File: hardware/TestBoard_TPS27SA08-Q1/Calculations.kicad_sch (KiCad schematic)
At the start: 0 parts

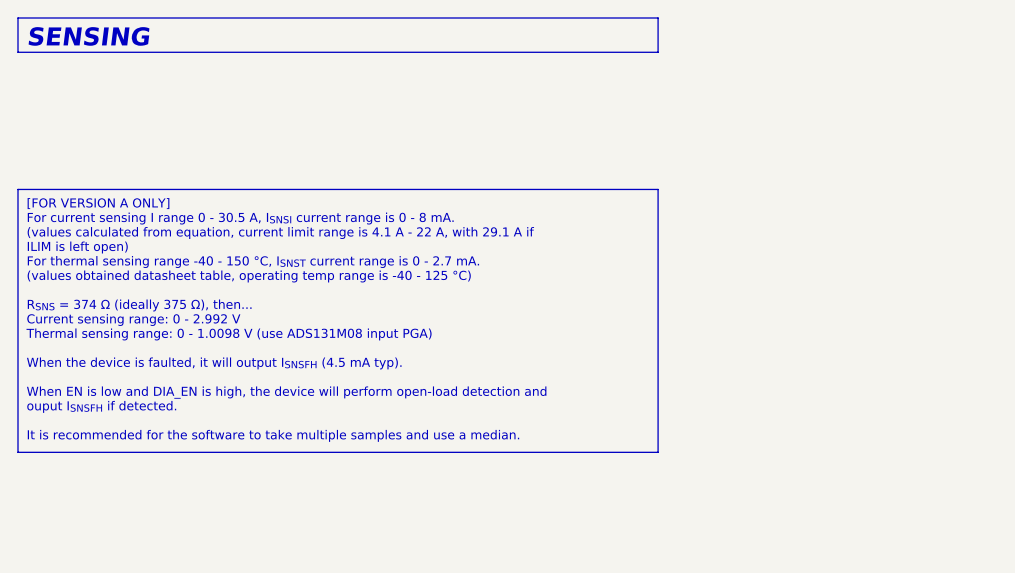
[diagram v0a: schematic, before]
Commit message: revisions (dip switch for address, leds on gpio outputs, logic analyzer pinout?, ...)
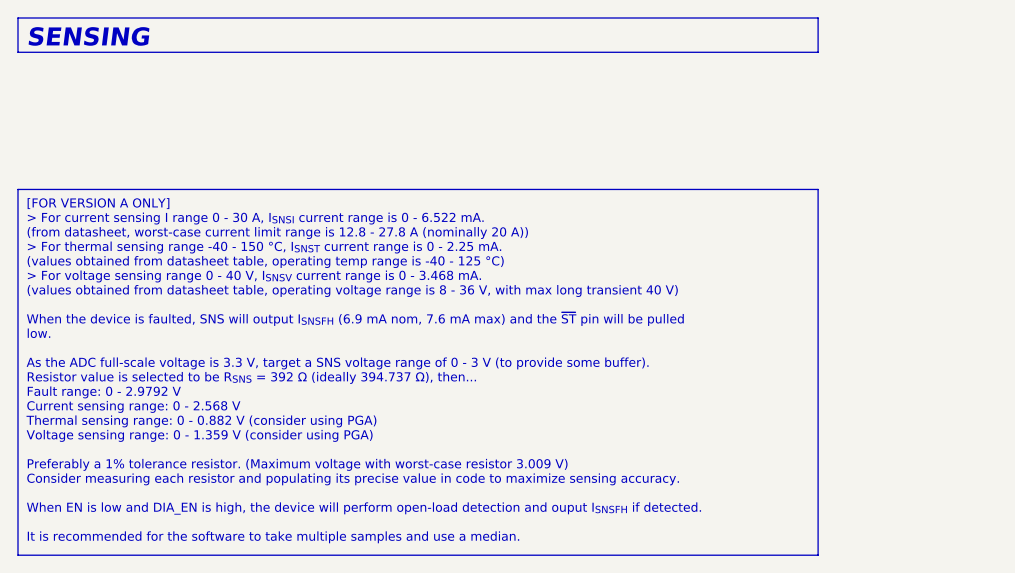
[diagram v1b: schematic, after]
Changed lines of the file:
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@@
 		(exclude_from_sim no)
 		(at 16.51 15.24 0)
-		(size 71.12 3.81)
+		(size 88.9 3.81)
 		(margins 0.9525 0.9525 0.9525 0.9525)
 		(stroke
@@
 		)
 	)
-	(text_box "[FOR VERSION A ONLY]\nFor current sensing I range 0 - 30.5 A, I_{SNSI} current range is 0 - 8 mA. \n(values calculated from equation, current limit range is 4.1 A - 22 A, with 29.1 A if ILIM is left open)\nFor thermal sensing range -40 - 150 °C, I_{SNST} current range is 0 - 2.7 mA. \n(values obtained datasheet table, operating temp range is -40 - 125 °C)\n\nR_{SNS} = 374 Ω (ideally 375 Ω), then...\nCurrent sensing range: 0 - 2.992 V\nThermal sensing range: 0 - 1.0098 V (use ADS131M08 input PGA)\n\nWhen the device is faulted, it will output I_{SNSFH} (4.5 mA typ). \n\nWhen EN is low and DIA_EN is high, the device will perform open-load detection and ouput I_{SNSFH} if detected.\n\nIt is recommended for the software to take multiple samples and use a median."
+	(text_box "[FOR VERSION A ONLY]\n> For current sensing I range 0 - 30 A, I_{SNSI} current range is 0 - 6.522 mA. \n  (from datasheet, worst-case current limit range is 12.8 - 27.8 A (nominally 20 A))\n> For thermal sensing range -40 - 150 °C, I_{SNST} current range is 0 - 2.25 mA. \n  (values obtained from datasheet table, operating temp range is -40 - 125 °C)\n> For voltage sensing range 0 - 40 V, I_{SNSV} current range is 0 - 3.468 mA. \n  (values obtained from datasheet table, operating voltage range is 8 - 36 V, with max long transient 40 V)\n\nWhen the device is faulted, SNS will output I_{SNSFH} (6.9 mA nom, 7.6 mA max) and the ~{ST} pin will be pulled low.\n\nAs the ADC full-scale voltage is 3.3 V, target a SNS voltage range of 0 - 3 V (to provide some buffer).\nResistor value is selected to be R_{SNS} = 392 Ω (ideally 394.737 Ω), then...\nFault range: 0 - 2.9792 V\nCurrent sensing range: 0 - 2.568 V\nThermal sensing range: 0 - 0.882 V (consider using PGA)\nVoltage sensing range: 0 - 1.359 V (consider using PGA)\n\nPreferably a 1% tolerance resistor. (Maximum voltage with worst-case resistor 3.009 V)\nConsider measuring each resistor and populating its precise value in code to maximize sensing accuracy.\n\nWhen EN is low and DIA_EN is high, the device will perform open-load detection and ouput I_{SNSFH} if detected.\n\nIt is recommended for the software to take multiple samples and use a median."
 		(exclude_from_sim no)
 		(at 16.51 34.29 0)
-		(size 71.12 29.21)
+		(size 88.9 40.64)
 		(margins 0.9525 0.9525 0.9525 0.9525)
 		(stroke
@@
 			)
 		)
-		(column_widths 6.35 7.62 21.59 35.56)
+		(column_widths 6.35 7.62 21.59 53.34)
 		(row_heights 2.54 2.54 2.54 5.08 2.54)
 		(cells
@@
 				(exclude_from_sim no)
 				(at 52.07 19.05 0)
-				(size 35.56 2.54)
+				(size 53.34 2.54)
 				(margins 0.9525 0.9525 0.9525 0.9525)
 				(span 1 1)
@@
 				)
 			)
-			(table_cell "CH1 Current"
+			(table_cell "Load Current"
 				(exclude_from_sim no)
 				(at 30.48 21.59 0)
@@
 				)
 			)
-			(table_cell "I_{SNSI} = I_{OUT} / K_{SNS}      K_{SNS} = 3000"
+			(table_cell "I_{SNSI} = I_{OUT} / K_{SNS}            K_{SNS} = 4600"
 				(exclude_from_sim no)
 				(at 52.07 21.59 0)
-				(size 35.56 5.08)
-				(margins 0.9525 0.9525 0.9525 0.9525)
-				(span 1 2)
+				(size 53.34 2.54)
+				(margins 0.9525 0.9525 0.9525 0.9525)
+				(span 1 1)
 				(fill
 					(type none)
@@
 				)
 			)
-			(table_cell "CH2 Current"
+			(table_cell "Not Used"
 				(exclude_from_sim no)
 				(at 30.48 24.13 0)
@@
 				(exclude_from_sim no)
 				(at 52.07 24.13 0)
-				(size 35.56 2.54)
-				(margins 0.9525 0.9525 0.9525 0.9525)
-				(span 0 0)
+				(size 53.34 2.54)
+				(margins 0.9525 0.9525 0.9525 0.9525)
+				(span 1 1)
 				(fill
 					(type none)
@@
 				)
 			)
-			(table_cell "I_{SNST} = (T_{J} - 25 [°C]) * dI_{SNST}/dT + 0.85      dI_{SNST}/dT = 0.011 [mA/°C]"
+			(table_cell "I_{SNST} = (T_{J} - 25 [°C]) * dI_{SNST}/dT + 0.85                  dI_{SNST}/dT = 0.0112 [mA/°C]"
 				(exclude_from_sim no)
 				(at 52.07 26.67 0)
-				(size 35.56 5.08)
+				(size 53.34 5.08)
 				(margins 0.9525 0.9525 0.9525 0.9525)
 				(span 1 1)
@@
 				)
 			)
-			(table_cell "X"
+			(table_cell "Supply Voltage"
 				(exclude_from_sim no)
 				(at 30.48 31.75 0)
@@
 				)
 			)
-			(table_cell ""
+			(table_cell "I_{SNSV} = (V_{BB}) * dI_{SNSV}/dV      K_{SNSV} = 0.0867"
 				(exclude_from_sim no)
 				(at 52.07 31.75 0)
-				(size 35.56 2.54)
-				(margins 0.9525 0.9525 0.9525 0.9525)
-				(span 1 1)
-				(fill
-					(type none)
-				)
-				(effects
-					(font
-						(size 1.27 1.27)
-					)
-					(justify left top)
+				(size 53.34 2.54)
+				(margins 0.9525 0.9525 0.9525 0.9525)
+				(span 1 1)
+				(fill
+					(type none)
+				)
+				(effects
+					(font
+						(size 1 1)
+					)
+					(justify left top)
